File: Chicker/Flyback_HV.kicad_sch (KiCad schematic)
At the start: 56 parts, among them Q2 IRFR3410TRPBF, Q3 FGH50T65SQD-F155, Q7 FGH50T65SQD-F155, T1 DA2034, U2 MCP14A0454-E/SN, U4 LT3750

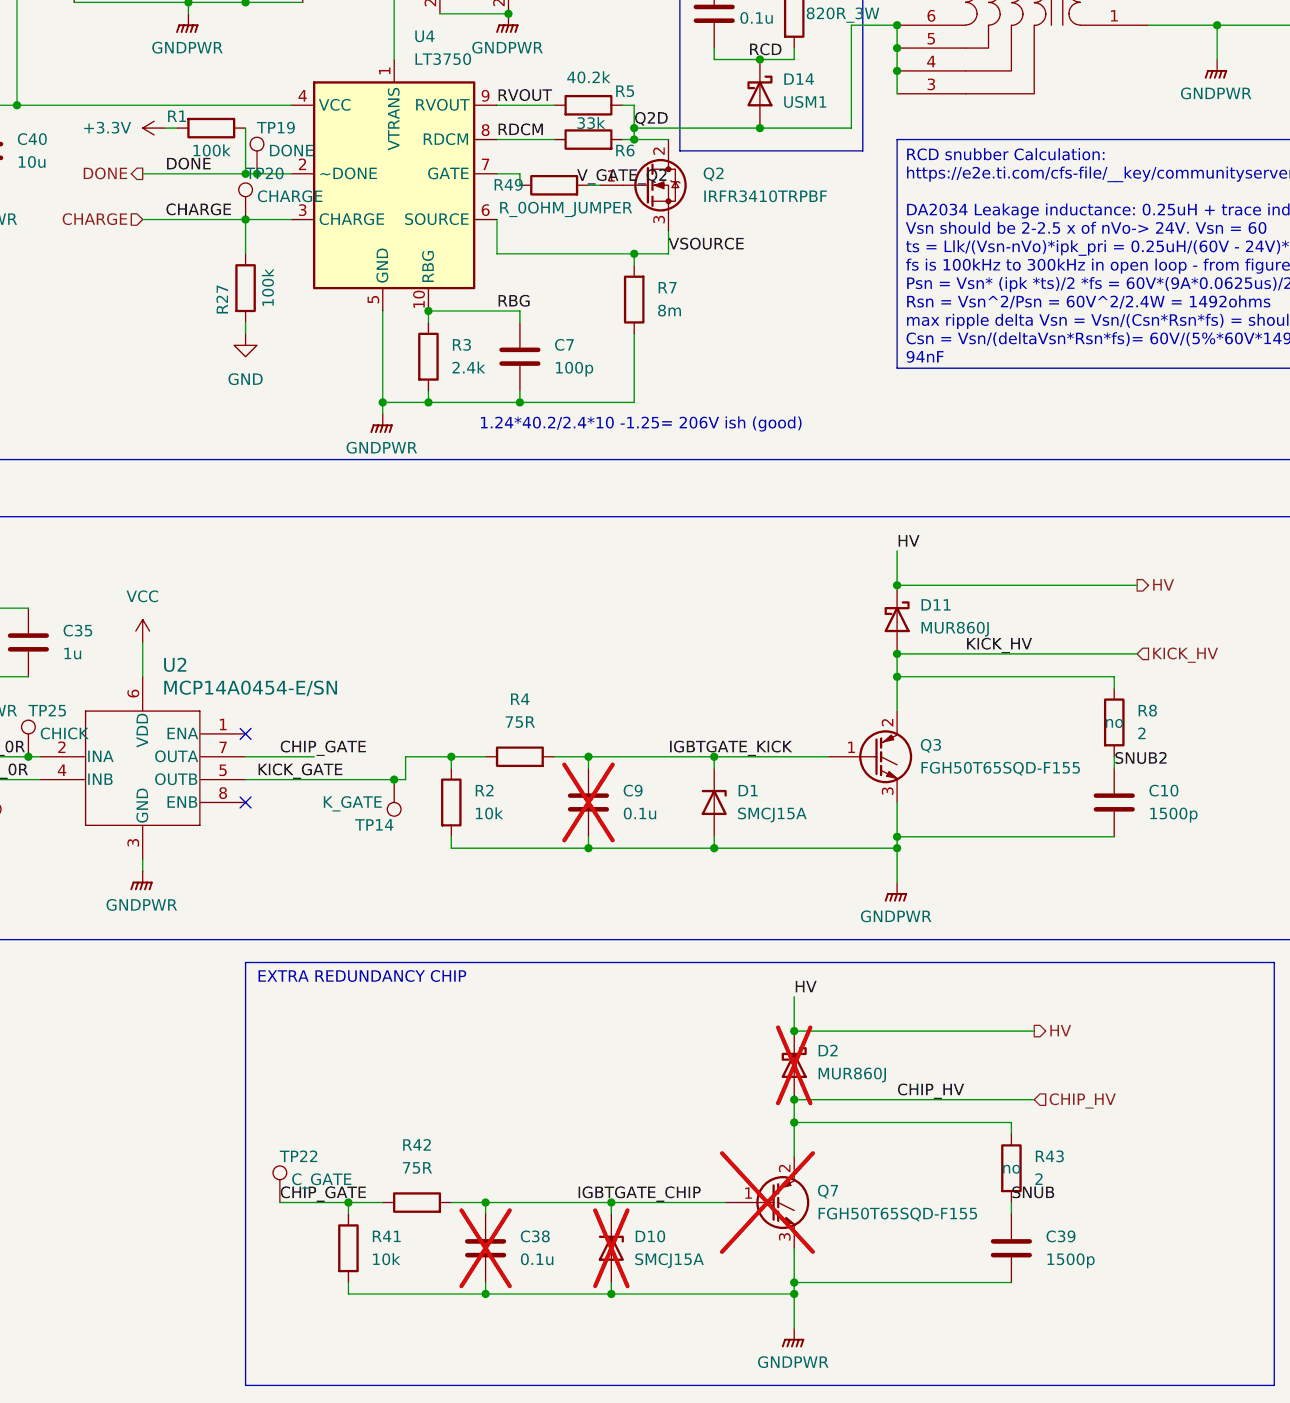
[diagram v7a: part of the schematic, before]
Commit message: changed more to basic
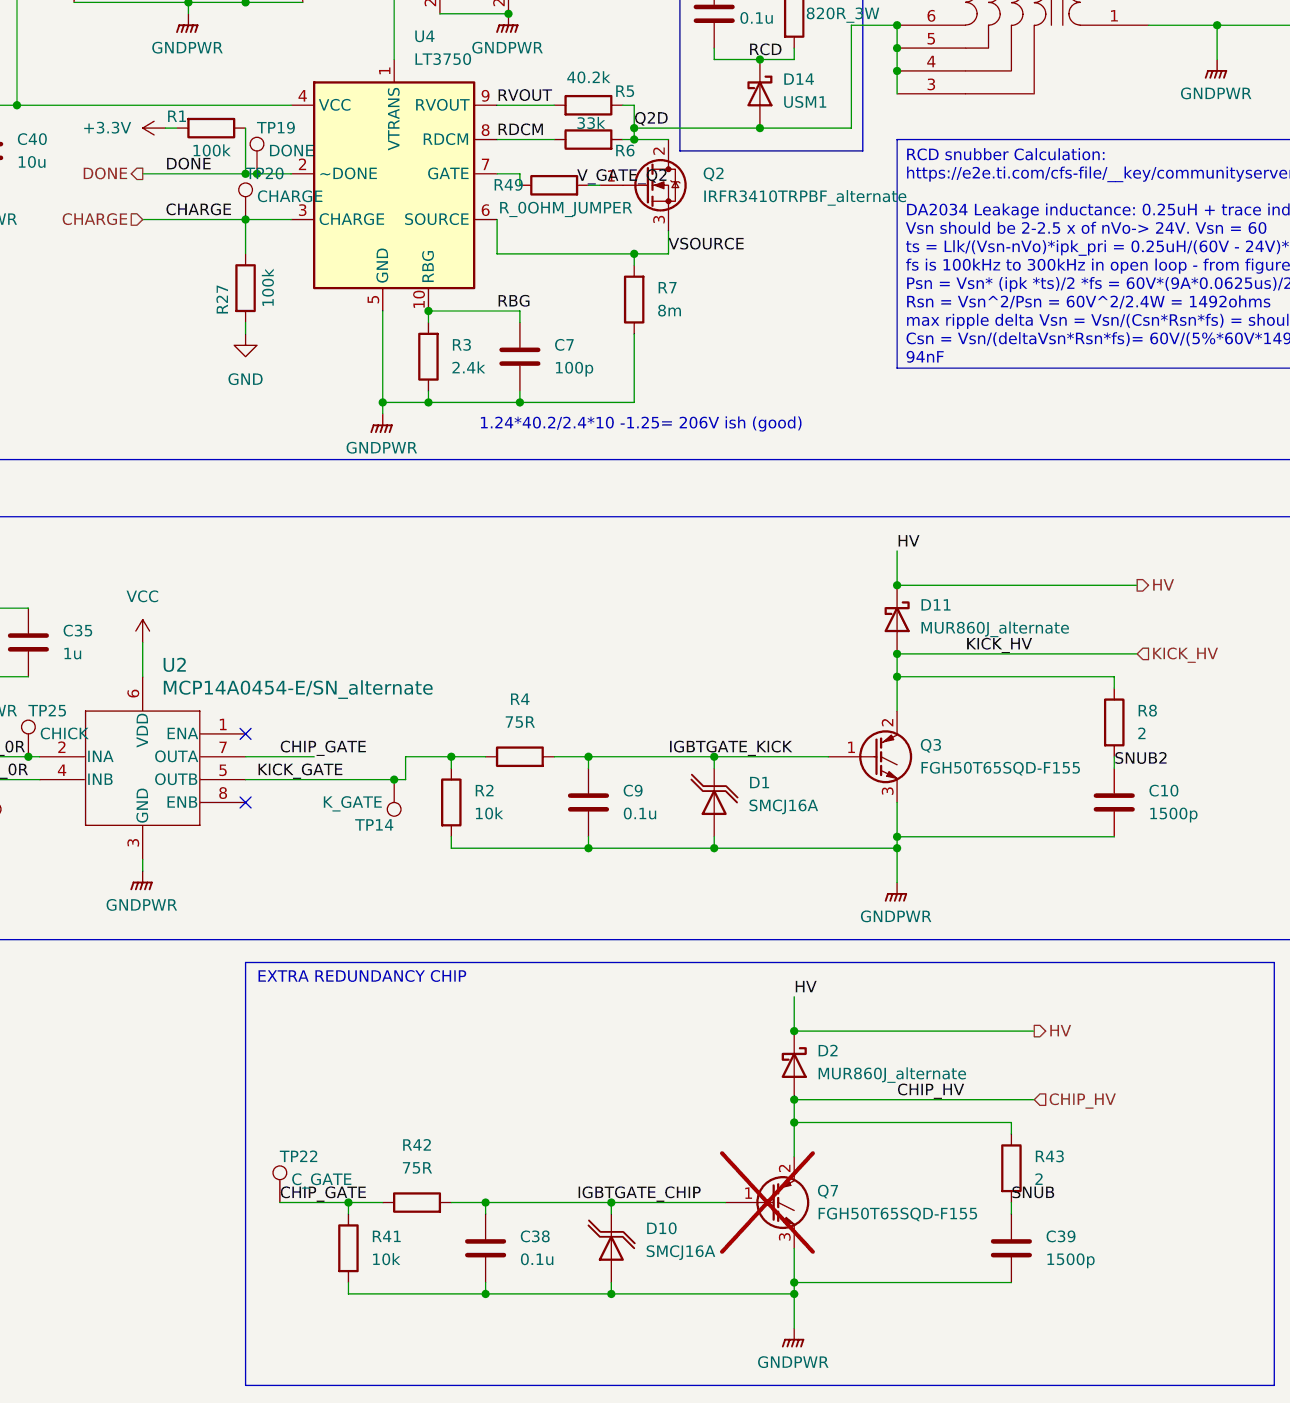
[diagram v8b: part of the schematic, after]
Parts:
- removed D1, D10: SMCJ15A, bots:D_SMC, symbol bots:SMCJ15A
- removed D11, D2: MUR860J, bots:D_SMC, symbol bots:MUR860J
- removed Q2: IRFR3410TRPBF, bots:DPAK-3_ONS, symbol bots:IRFR3410TRPBF
- removed U2: MCP14A0454-E/SN, bots:SOIC-8_3.9x4.9mm_P1.27mm, symbol bots:MCP14A0454-E_SN
- added D1, D10: SMCJ16A, bots:D_SMC, symbol bots:D_SMCJ16A
- added D11, D2: MUR860J_alternate, bots:D_SMC, symbol bots:D_MUR860J_alternate
- added Q2: IRFR3410TRPBF_alternate, bots:DPAK-3_ONS, symbol bots:Q_IRFR3410TRPBF_alternate
- added U2: MCP14A0454-E/SN_alternate, bots:SOIC-8_3.9x4.9mm_P1.27mm, symbol bots:MCP14A0454-E_SN_alternate
- C1, C2: LCSC C136279 -> C33129640
- C38, C9: now fitted; now in the parts list
- Q3: now left out of the parts list
- U4: JLC Extended (none) -> yes
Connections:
- net CHIP_0R: now also U2.2 (INA)
- net CHIP_GATE: now also U2.7 (OUTA)
- net CHIP_HV: now also D2.2 (A)
- net GNDPWR: now also R3.1, D1.2 (A), D10.2 (A), U2.3 (GND); no longer R3.2
- net HV: now also D11.1 (K), D2.1 (K)
- net IGBTGATE_CHIP: now also D10.1 (K)
- net IGBTGATE_KICK: now also D1.1 (K)
- net KICK_0R: now also U2.4 (INB)
- net KICK_GATE: now also U2.5 (OUTB)
- net KICK_HV: now also D11.2 (A)
- net Q2D: now also Q2.2 (D)
- net RBG: now also R3.2; no longer R3.1
- net VCC: now also U2.6 (VDD)
- net VSOURCE: now also Q2.3 (S)
- net at R49.2: now also Q2.1 (G)
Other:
- moved on the sheet: R3
